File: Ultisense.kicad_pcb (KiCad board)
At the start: 2 copper layers, 74 parts, among them J1 USB_C_Receptacle_USB2.0_14P, J2 Conn_01x02, J3 Micro_SD_Card, J5 Conn_01x08, J6 Conn_02x02_Odd_Even, J7 Conn_02x08_Top_Bottom, J8 Conn_01x08, SW2 SW_Push, SW3 SW_Push, U1 ESP32-S3-WROOM-1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

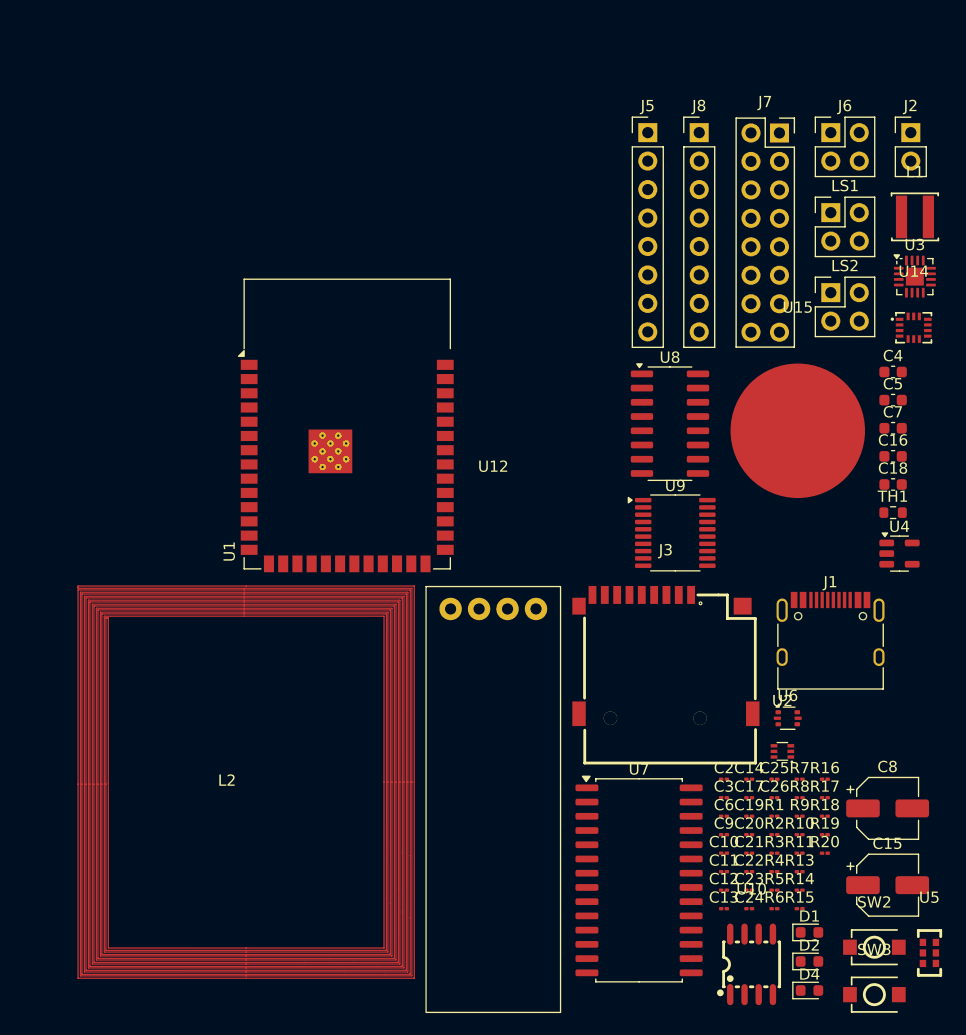
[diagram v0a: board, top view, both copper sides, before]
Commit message: actually fr done schematic, figured out nfc antenna
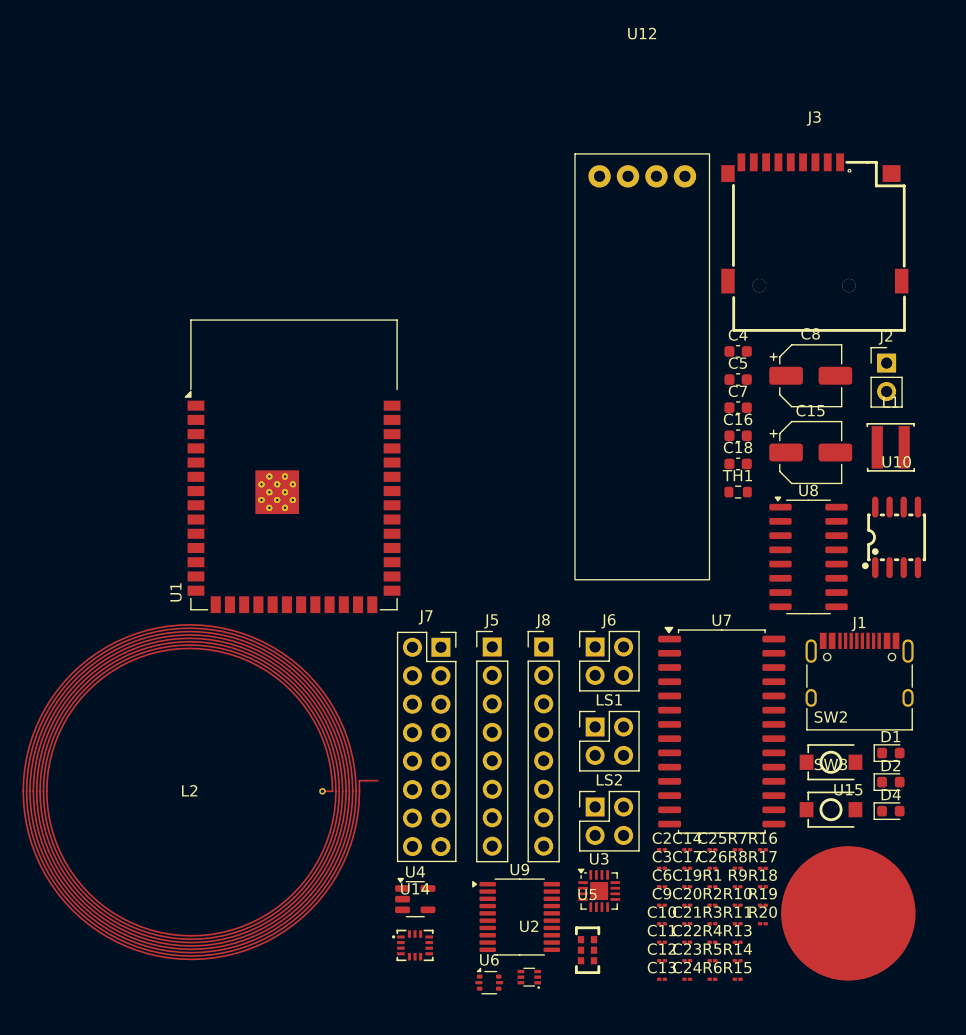
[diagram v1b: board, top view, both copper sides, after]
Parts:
- L2: footprint nfc:nfcantenna -> PCB Coils:NFC_Coil
- moved U14 70.8 mm to (50.7, 95.2)
- moved U3 61.6 mm to (67.1, 90.3)
- moved J7 54.9 mm to (53.0, 68.5)
- moved U4 53.1 mm to (50.7, 91.0)
- moved J6 50.5 mm to (66.7, 68.5)
- moved LS1 50.5 mm to (66.7, 75.7)
- moved LS2 50.5 mm to (66.7, 82.8)
- moved J5 47.9 mm to (57.5, 68.5)
- moved J8 47.9 mm to (62.1, 68.5)
- moved U15 43.3 mm to (89.3, 92.3)
- moved J3 40.8 mm to (86.3, 30.6)
- moved U12 40.8 mm to (70.9, 26.5)
- moved U10 40.2 mm to (93.6, 58.7)
- moved C15 39.2 mm to (86.0, 51.2)
- moved C8 39.2 mm to (86.0, 44.3)
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
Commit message: layout done
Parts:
- removed C22: 1uF, Capacitor_SMD:C_01005_0402Metric
- added C27: 0.1uF, Capacitor_SMD:C_01005_0402Metric, F.Cu at (157.2, 81.0)
- added C28: 0.1uF, Capacitor_SMD:C_01005_0402Metric, F.Cu at (157.3, 77.8)
- added C29: 0.1uF, Capacitor_SMD:C_01005_0402Metric, F.Cu at (161.4, 80.4)
- added C30: 0.1uF, Capacitor_SMD:C_01005_0402Metric, F.Cu at (150.1, 80.8)
- added C31: 1uF, Capacitor_SMD:C_01005_0402Metric, F.Cu at (156.6, 77.8)
- added C32: 1uF, Capacitor_SMD:C_01005_0402Metric, F.Cu at (158.2, 124.4)
- added C33: 1uF, Capacitor_SMD:C_01005_0402Metric, F.Cu at (154.2, 81.7)
- added C34: 0.1uF, Capacitor_SMD:C_01005_0402Metric, F.Cu at (144.7, 128.1)
- added C36: 0.1uF, Capacitor_SMD:C_01005_0402Metric, F.Cu at (132.1, 99.1)
- added U11: SHT41I-AD1B-R2, easyeda2kicad:SENSOR-SMD_4P-L1.5-W1.5-P1.00-TL, F.Cu at (155.6, 80.2)
- added U13: QMC6309, easyeda2kicad:X1-WLB0808-4_L0.8-W0.8-P0.40-TL, F.Cu at (158.3, 77.2)
- added U16: OPT4048DTSR, easyeda2kicad:SOT-5X3-8_L2.1-W1.2-P0.50-LS1.9-BL, F.Cu at (159.7, 79.2)
- added U17: SGP40-D-R4, easyeda2kicad:DFN-6_L2.4-W2.4-P0.80-TL-EP, F.Cu at (152.2, 81.3)
- LS1, LS2: footprint Connector_PinHeader_2.54mm:PinHeader_2x02_P2.54mm_Vertical -> Connector_PinHeader_2.54mm:PinHeader_2x01_P2.54mm_Vertical
- moved U12 130.4 mm to (162.4, 119.5), turned to 90 degrees
- moved L2 125.2 mm to (154.6, 98.7), turned to -90 degrees
- moved J3 125.2 mm to (158.2, 133.1)
- moved U1 113.7 mm to (153.6, 52.5)
- moved C4 107.6 mm to (148.7, 124.6), turned to 90 degrees
- moved C5 103.6 mm to (142.7, 126.8), turned to -90 degrees
- moved U14 103.5 mm to (152.5, 77.1)
- moved TH1 100.5 mm to (149.4, 126.9)
- moved J2 100.1 mm to (151.2, 124.4), turned to 180 degrees
- moved C7 97.1 mm to (135.7, 126.4), turned to 90 degrees
- moved U6 93.1 mm to (144.6, 130.7), turned to 90 degrees
- moved C8 90.9 mm to (133.4, 121.9), turned to -90 degrees
- moved U5 90.3 mm to (153.5, 73.0)
- moved U4 90.3 mm to (132.8, 128.3), turned to 180 degrees
- moved LS1 89.9 mm to (136.9, 131.9), turned to -90 degrees
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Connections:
- net Net-(J1-D+-PadA6) renamed /D+
- net Net-(J1-D--PadA7) renamed /D-
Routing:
- net GPB1: track 0.00 -> 39.5 mm
- net GPB2: track 0.00 -> 36.8 mm
- net GPB4: track 0.00 -> 34.0 mm
- net GPB3: track 0.00 -> 32.3 mm
- net GPB5: track 0.00 -> 29.5 mm
- net +5V: track 0.00 -> 25.8 mm
- net GPB7: track 0.00 -> 25.3 mm
- net GPB6: track 0.00 -> 21.9 mm
- net +3V3: track 0.00 -> 21.4 mm
- net VBUS: track 0.00 -> 20.2 mm
- net GPB0: track 0.00 -> 13.4 mm, vias 0 -> 1
- net Net-(U2-EN): track 0.00 -> 8.71 mm
- net Net-(U8-INL): track 0.00 -> 8.61 mm
- net GPA5: track 0.00 -> 7.14 mm
- net GPA1: track 0.00 -> 7.14 mm
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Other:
- board outline added: 42.8 x 93.9 mm

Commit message: routing almost done; backup:
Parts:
- removed J8: Conn_01x08, Connector_PinHeader_2.54mm:PinHeader_1x08_P2.54mm_Vertical
- J5: value Conn_01x08 -> Conn_02x08_Odd_Even; footprint Connector_PinHeader_2.54mm:PinHeader_1x08_P2.54mm_Vertical -> Connector_PinHeader_2.54mm:PinHeader_2x08_P2.54mm_Vertical
- moved LS2 5.07 mm to (137.1, 135.3), turned to 90 degrees
- moved LS1 4.77 mm to (133.5, 135.3), turned to 90 degrees
- moved C3 1.50 mm to (146.0, 128.1), turned to 0 degrees
- moved R3 0.90 mm to (147.7, 128.2)
- moved R14 0.52 mm to (134.8, 72.5), turned to -90 degrees
- moved J5 0.36 mm to (130.1, 47.8)
- moved R15 0.26 mm to (159.6, 126.2)
- moved R18 0.26 mm to (158.3, 126.2)
- moved R19 0.26 mm to (156.1, 126.2)
- moved R20 0.26 mm to (153.9, 126.2)
- moved J3 0.26 mm to (158.2, 132.8)
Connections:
- J5 pad 1: IO21 -> TXD0
- J5 pad 2: IO18 -> RXD0
- J5 pad 3: MISO -> IO41
- J5 pad 4: SCK -> IO42
- J5 pad 5: MOSI -> IO39
- J5 pad 6: IO7 -> IO40
- J5 pad 7: SCL -> IO7
- J5 pad 8: SDA -> IO38
- U9 pad 10: Net-(U9-DEMP) -> GND
- U9 pad 11: Net-(U9-DEMP) -> GND
- U9 pad 12: Net-(U9-DEMP) -> GND
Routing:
- net +3V3: track 21.4 -> 302.5 mm, vias 0 -> 18
- net SDA: track 0.00 -> 138.6 mm, vias 0 -> 6
- net MISO: track 1.38 -> 111.8 mm, vias 0 -> 3
- net MOSI: track 1.38 -> 110.4 mm, vias 0 -> 3
- net SCK: track 1.38 -> 110.0 mm, vias 0 -> 3
- net SCL: track 0.00 -> 105.9 mm, vias 0 -> 8
- net USB_D-: track 0.00 -> 101.6 mm, vias 0 -> 2
- net USB_D+: track 0.00 -> 101.5 mm, vias 0 -> 2
- net IO48: track 0.00 -> 82.3 mm, vias 0 -> 2
- net IO10: track 1.30 -> 73.4 mm, vias 0 -> 2
- net IO15: track 0.00 -> 66.3 mm, vias 0 -> 2
- net IO1: track 0.00 -> 57.4 mm
- net IO16: track 0.00 -> 56.5 mm, vias 0 -> 4
- net IO6: track 0.00 -> 56.4 mm, vias 0 -> 4
- net IO2: track 0.00 -> 55.1 mm
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- added copper zone on B.Cu, net GND
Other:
- board size 42.8 x 93.9 mm -> 42.8 x 93.6 mm
- copper layers 2 -> 4

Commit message: routing done !!
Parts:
- moved C25 0.44 mm to (155.0, 77.8), turned to 0 degrees
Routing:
- net +3V3: track 302.5 -> 312.0 mm
- net MOSI: track 110.4 -> 113.6 mm
- net GPB2: track 36.8 -> 39.3 mm
- net IO10: track 73.4 -> 75.8 mm
- net GPB3: track 32.3 -> 34.3 mm
- net GPB4: track 34.0 -> 35.6 mm
- net GPB7: track 25.3 -> 26.9 mm
- net IO14: track 48.5 -> 50.0 mm
- net GPB6: track 21.9 -> 23.3 mm
- net IO16: track 56.5 -> 57.7 mm
- net GPB5: track 29.5 -> 30.7 mm
- net Net-(U2-EN): track 8.71 -> 9.68 mm
- net IO40: track 31.1 -> 32.0 mm
- net IO6: track 56.4 -> 57.0 mm
- net MISO: track 111.8 -> 112.4 mm
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- added copper zone on F.Cu, net GND
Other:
- copper layers 4 -> 2

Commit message: done
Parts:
- C4, C5, C7: value 4.7uF -> 10uF
- R13: value 330 -> 470
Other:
- board text added: ":)"
- board text added: "NFC"
- board text added: "TOUCH"
- board text added: "by darsh !!"

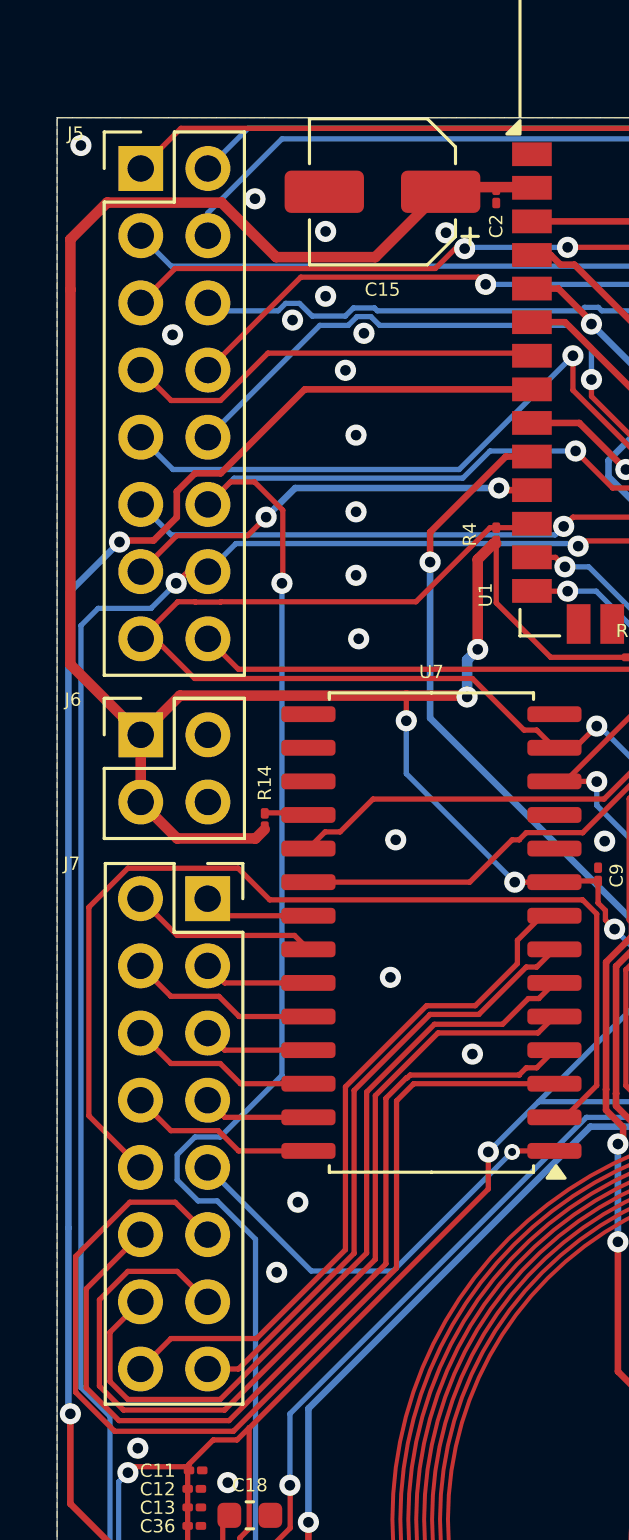
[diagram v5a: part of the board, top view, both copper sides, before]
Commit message: headers silkscreen
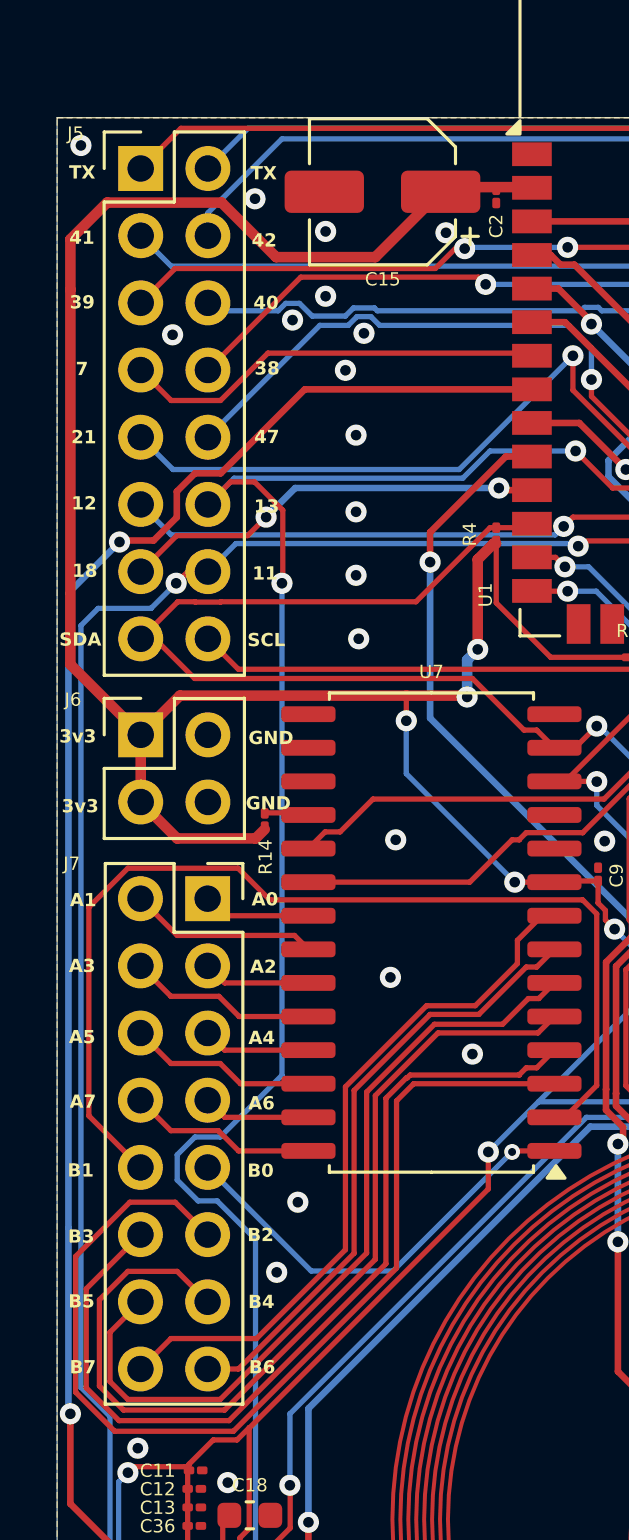
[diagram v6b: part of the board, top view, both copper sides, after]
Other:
- board text added: "11"
- board text added: "12"
- board text added: "13"
- board text added: "18"
- board text added: "21"
- board text added: "38"
- board text added: "39"
- board text added: "3v3"
- board text added: "40"
- board text added: "41"
- board text added: "42"
- board text added: "47"
- board text added: "7"
- board text added: "A0"
- board text added: "A1"
- board text added: "A2"
- board text added: "A3"
- board text added: "A4"
- board text added: "A5"
- board text added: "A6"
- board text added: "A7"
- board text added: "B0"
- board text added: "B1"
- board text added: "B2"
- board text added: "B3"
- board text added: "B4"
- board text added: "B5"
- board text added: "B6"
- board text added: "B7"
- board text added: "GND"
- board text added: "SCL"
- board text added: "SDA"
- board text added: "TX"

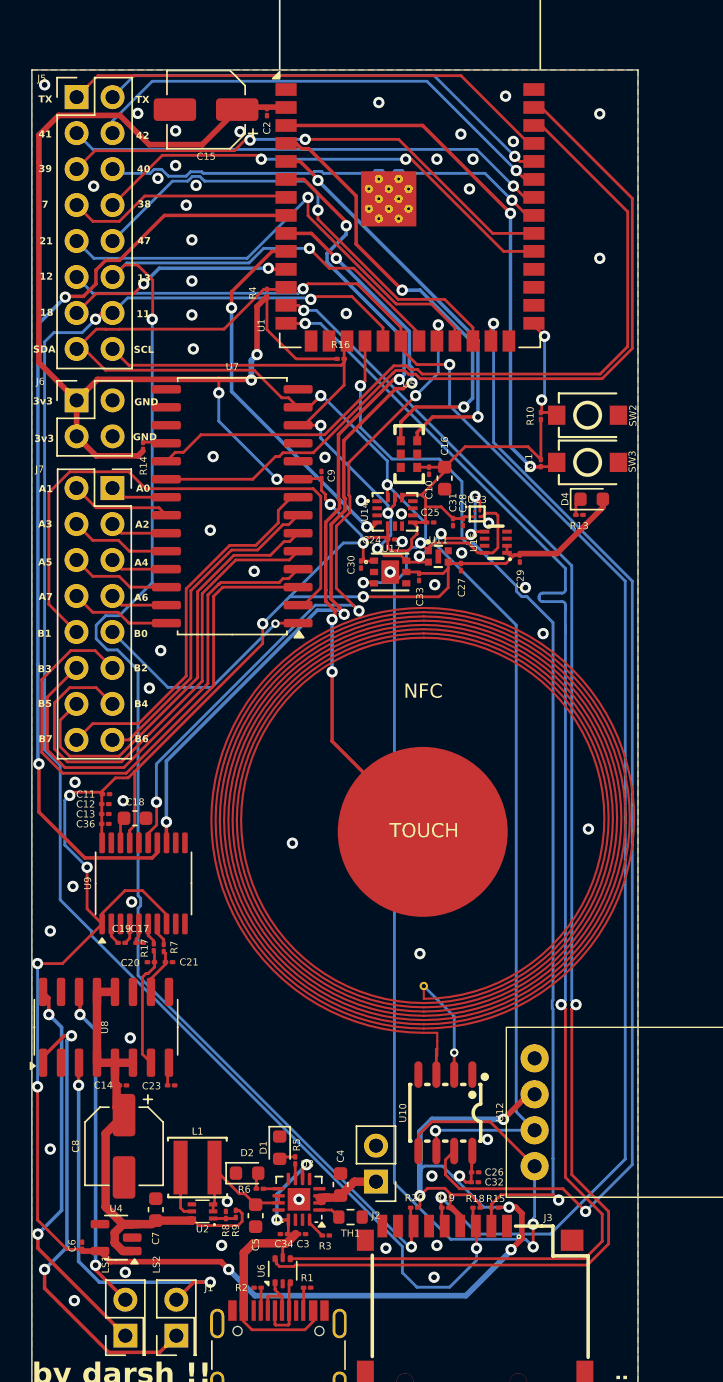
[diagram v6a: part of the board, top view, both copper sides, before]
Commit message: added test points and changed silkscreen
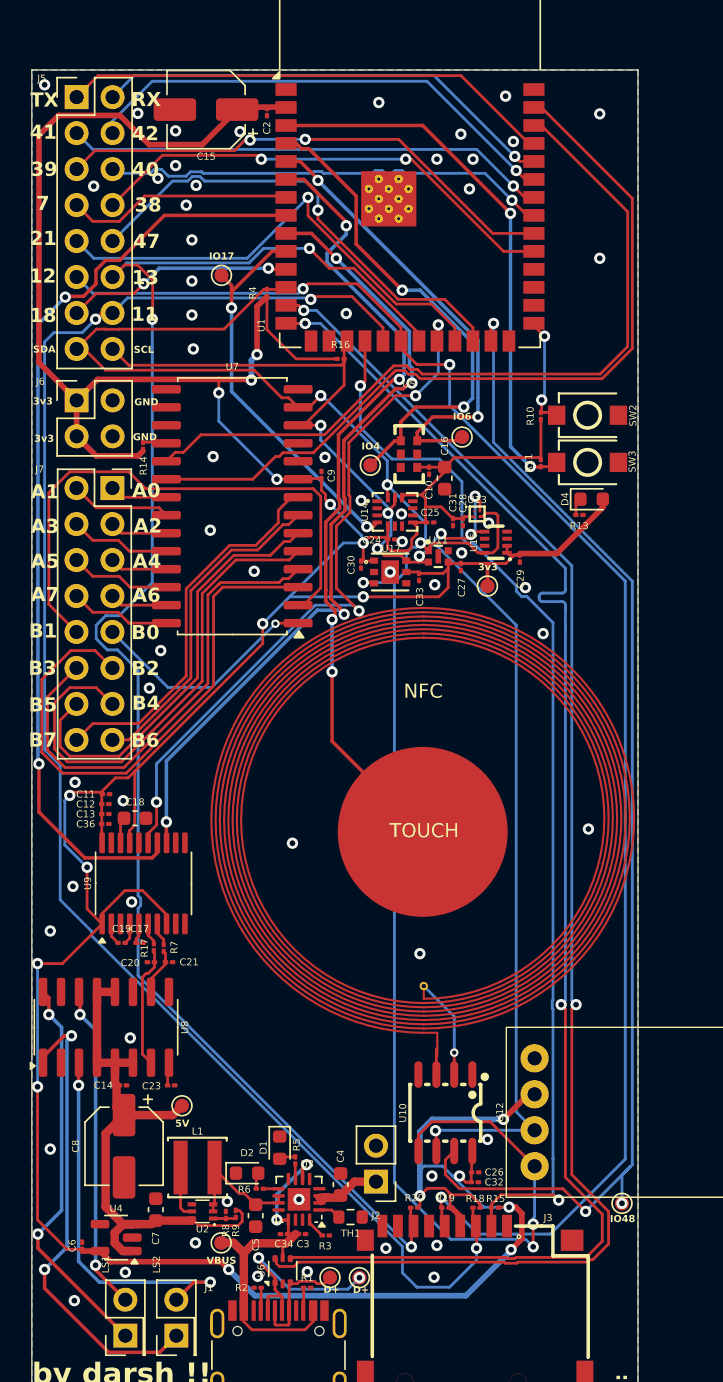
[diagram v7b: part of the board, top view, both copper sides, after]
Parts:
- added 3v3: TestPoint_Pad_D1.0mm, TestPoint:TestPoint_Pad_D1.0mm, F.Cu at (159.1, 82.3)
- added 5V: TestPoint_Pad_D1.0mm, TestPoint:TestPoint_Pad_D1.0mm, F.Cu at (137.5, 119.0)
- added D+: TestPoint_Pad_D1.0mm, TestPoint:TestPoint_Pad_D1.0mm, F.Cu at (147.9, 131.2)
- added D+: TestPoint_Pad_D1.0mm, TestPoint:TestPoint_Pad_D1.0mm, F.Cu at (150.0, 131.2)
- added IO17: TestPoint_Pad_D1.0mm, TestPoint:TestPoint_Pad_D1.0mm, F.Cu at (140.3, 60.4)
- added IO4: TestPoint_Pad_D1.0mm, TestPoint:TestPoint_Pad_D1.0mm, F.Cu at (150.8, 73.8)
- added IO48: TestPoint_Pad_D1.0mm, TestPoint:TestPoint_Pad_D1.0mm, F.Cu at (168.6, 125.9)
- added IO6: TestPoint_Pad_D1.0mm, TestPoint:TestPoint_Pad_D1.0mm, F.Cu at (157.3, 71.8)
- added VBUS: TestPoint_Pad_D1.0mm, TestPoint:TestPoint_Pad_D1.0mm, F.Cu at (140.3, 128.7)
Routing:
- net /D-: track 4.18 -> 14.8 mm, vias 0 -> 2
- net +5V: track 35.2 -> 39.5 mm
- net IO5: track 29.6 -> 32.9 mm
- net /D+: track 5.50 -> 8.64 mm
- net IO4: track 32.0 -> 34.9 mm
- net IO48: track 82.3 -> 85.2 mm, vias 2 -> 3
- net VBUS: track 24.9 -> 26.8 mm
- net IO17: track 26.4 -> 27.9 mm
- net +3V3: track 312.0 -> 313.0 mm
- net IO14: track 50.0 -> 50.8 mm
- net GND: vias 58 -> 60
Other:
- board text added: "RX"

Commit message: fixed nfc
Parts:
- removed U15: ~, touchpad:Touch_Pad
- added IO6: TestPoint_Pad_D1.0mm, TestPoint:TestPoint_Pad_D1.0mm, F.Cu at (141.4, 53.4)
- moved U12 15.0 mm to (169.5, 132.7)
- moved IO48 1.64 mm to (168.7, 124.3)
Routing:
- net IO6: track 57.0 -> 3.61 mm, vias 4 -> 0
- net SCL: track 105.9 -> 144.6 mm, vias 8 -> 11
- net SDA: track 138.2 -> 162.2 mm, vias 6 -> 8
- net +3V3: track 313.0 -> 303.6 mm, vias 18 -> 15
- net IO1: track 57.4 -> 50.2 mm
- net IO2: track 55.1 -> 48.3 mm
- net IO10: track 75.8 -> 80.0 mm
- net USB_D-: track 101.7 -> 105.0 mm
- net USB_D+: track 101.6 -> 104.6 mm
- net IO14: track 50.8 -> 48.3 mm
- net IO16: track 57.7 -> 55.2 mm
- net SCK: track 110.0 -> 111.4 mm, vias 3 -> 5
- net IO48: track 85.2 -> 83.8 mm, vias 3 -> 4
- net GPB2: track 39.3 -> 40.4 mm
- net GND: vias 60 -> 61
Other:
- board size 42.8 x 93.6 mm -> 44.7 x 93.6 mm
- board text removed: "TOUCH"
